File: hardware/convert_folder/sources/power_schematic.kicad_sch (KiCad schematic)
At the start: 33 parts, among them CN1 5-146285-2, CN11 5-146285-2, CN13 4243-0, CN15 JST 2 position header 2.5mm, CN2 4243-0, CN3 4 pin Picoblade, CN7 5-146285-2, CN8 5-146285-2, CN9 5-146285-2, IC1 TPS3780BDBVT, J3 USB-C, J8 87832-1420, J9 87832-1420, SW1 SW-T3-2B-A-A3-S1

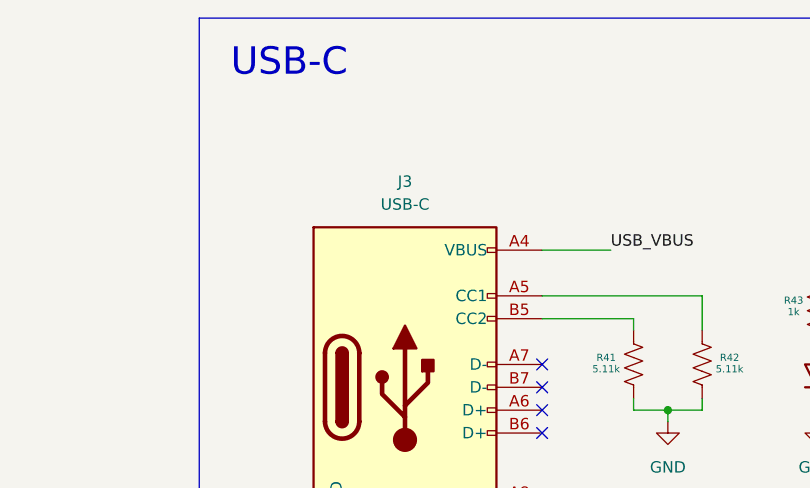
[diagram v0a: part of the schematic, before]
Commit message: fix: fix some footprints and the position of refs. in the layout
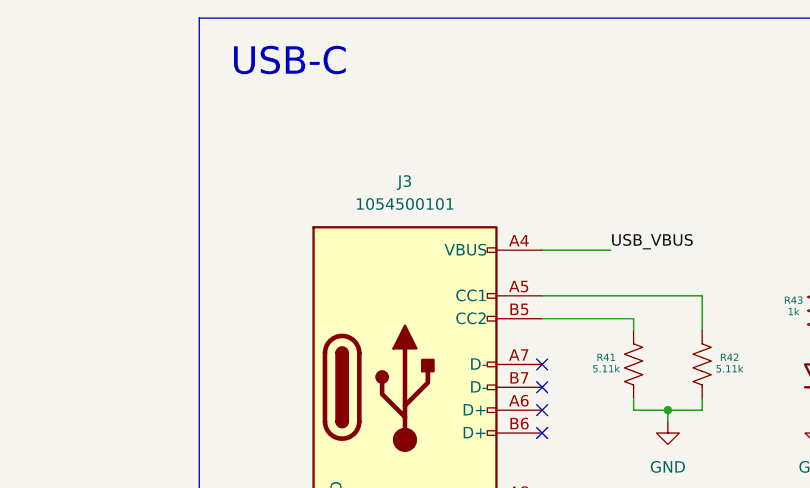
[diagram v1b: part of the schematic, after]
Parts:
- removed J3: USB-C, altium_import:FP-1054500101-MFG, symbol connectors:USB-C
- added J3: 1054500101, altium_import:FP-1054500101-MFG, symbol lib:1054500101
- R41, R42: footprint footprints:RES0402 -> lib:RES0402
- R43: footprint footprints:RES0603 -> lib:RES0603
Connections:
- net GND: now also J3.A1 (GND), J3.A12 (GND), J3.B1 (GND), J3.B12 (GND), J3.S1 (SHIELD)
- net USB_VBUS: now also J3.A4 (VBUS), J3.A9 (VBUS), J3.B4 (VBUS), J3.B9 (VBUS)
- net at R41.2: now also J3.B5 (CC2)
- net at R42.2: now also J3.A5 (CC1)
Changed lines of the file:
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@@
 	(text_box "USB-C"
 		(exclude_from_sim no)
-		(at 242.18 35.941 0)
-		(size -36.44 8.128)
+		(at 205.74 35.941 0)
+		(size 36.44 8.128)
 		(margins 0.9525 0.9525 0.9525 0.9525)
 		(stroke
@@
 			)
 		)
-		(property "Footprint" "footprints:RES0402"
+		(property "Footprint" "lib:RES0402"
 			(at 245.11 50.292 0)
 			(effects
@@
 	)
 	(symbol
-		(lib_id "connectors:USB-C")
-		(at 226.06 74.93 0)
-		(unit 1)
-		(exclude_from_sim no)
-		(in_bom yes)
-		(on_board yes)
-		(dnp no)
-		(fields_autoplaced yes)
-		(property "Reference" "J3"
-			(at 226.06 52.07 0)
-			(effects
-				(font
-					(size 1.27 1.27)
-				)
-			)
-		)
-		(property "Value" "USB-C"
-			(at 226.06 54.61 0)
-			(effects
-				(font
-					(size 1.27 1.27)
-				)
-			)
-		)
-		(property "Footprint" "altium_import:FP-1054500101-MFG"
-			(at 229.87 72.39 0)
-			(effects
-				(font
-					(size 1.27 1.27)
-				)
-				(hide yes)
-			)
-		)
-		(property "Datasheet" "https://www.usb.org/sites/default/files/documents/usb_type-c.zip"
-			(at 273.304 97.028 0)
-			(effects
-				(font
-					(size 1.27 1.27)
-				)
-				(hide yes)
-			)
-		)
-		(property "Description" "USB Power-Only 6P Type-C Receptacle connector"
-			(at 265.684 93.98 0)
-			(effects
-				(font
-					(size 1.27 1.27)
-				)
-				(hide yes)
-			)
-		)
-		(property "Arrow Part Number" ""
-			(at 226.06 74.93 0)
-			(effects
-				(font
-					(size 1.27 1.27)
-				)
-				(hide yes)
-			)
-		)
-		(property "Arrow Price/Stock" ""
-			(at 226.06 74.93 0)
-			(effects
-				(font
-					(size 1.27 1.27)
-				)
-				(hide yes)
-			)
-		)
-		(property "Height" ""
-			(at 226.06 74.93 0)
-			(effects
-				(font
-					(size 1.27 1.27)
-				)
-				(hide yes)
-			)
-		)
-		(property "Manufacturer_Name" ""
-			(at 226.06 74.93 0)
-			(effects
-				(font
-					(size 1.27 1.27)
-				)
-				(hide yes)
-			)
-		)
-		(property "Manufacturer_Part_Number" ""
-			(at 226.06 74.93 0)
-			(effects
-				(font
-					(size 1.27 1.27)
-				)
-				(hide yes)
-			)
-		)
-		(property "Mouser Part Number" ""
-			(at 226.06 74.93 0)
-			(effects
-				(font
-					(size 1.27 1.27)
-				)
-				(hide yes)
-			)
-		)
-		(property "Mouser Price/Stock" ""
-			(at 226.06 74.93 0)
-			(effects
-				(font
-					(size 1.27 1.27)
-				)
-				(hide yes)
-			)
-		)
-		(property "MPN" "UJ20-C-H-G-MSMT-4B-P16-TR"
-			(at 226.06 74.93 0)
-			(effects
-				(font
-					(size 1.27 1.27)
-				)
-				(hide yes)
-			)
-		)
-		(pin "A9"
-		)
-		(pin "S1"
-		)
-		(pin "B12"
-		)
-		(pin "A12"
-		)
-		(pin "B9"
-		)
-		(pin "A5"
-		)
-		(pin "B5"
-		)
-		(pin "B7"
-		)
-		(pin "A6"
-		)
-		(pin "B6"
-		)
-		(pin "A4"
-		)
-		(pin "B4"
-		)
-		(pin "B1"
-		)
-		(pin "A7"
-		)
-		(pin "A1"
-		)
-		(pin "A8"
-		)
-		(pin "B8"
-		)
-		(instances
-			(project "flatsat_platform_2"
-				(path "/8c88a7e1-4137-48d7-b926-b5e762e3852f/8386d232-e6d5-4b15-8289-83f2ee4d46fe"
-					(reference "J3")
-					(unit 1)
-				)
-			)
-		)
-	)
-	(symbol
 		(lib_id "resistors:CRCW06031K00FKEAHP")
 		(at 271.78 66.04 90)
@@
 			)
 		)
-		(property "Footprint" "footprints:RES0603"
+		(property "Footprint" "lib:RES0603"
 			(at 265.43 43.942 0)
 			(effects
@@
 			)
 		)
-		(property "Footprint" "footprints:RES0402"
+		(property "Footprint" "lib:RES0402"
 			(at 252.73 50.292 0)
 			(effects
@@
 					(unit 1)
 				)
+			)
+		)
+	)
+	(symbol
+		(lib_id "lib:1054500101")
+		(at 226.06 74.93 0)
+		(unit 1)
+		(exclude_from_sim no)
+		(in_bom yes)
+		(on_board yes)
+		(dnp no)
+		(fields_autoplaced yes)
+		(property "Reference" "J3"
+			(at 226.06 52.07 0)
+			(effects
+				(font
+					(size 1.27 1.27)
+				)
+			)
+		)
+		(property "Value" "1054500101"
+			(at 226.06 54.61 0)
+			(effects
+				(font
+					(size 1.27 1.27)
+				)
+			)
+		)
+		(property "Footprint" "altium_import:FP-1054500101-MFG"
+			(at 229.87 72.39 0)
+			(effects
+				(font
+					(size 1.27 1.27)
+				)
+				(hide yes)
+			)
+		)
+		(property "Datasheet" "https://www.usb.org/sites/default/files/documents/usb_type-c.zip"
+			(at 273.304 97.028 0)
+			(effects
+				(font
+					(size 1.27 1.27)
+				)
+				(hide yes)
+			)
+		)
+		(property "Description" "USB Power-Only 6P Type-C Receptacle connector"
+			(at 265.684 93.98 0)
+			(effects
+				(font
+					(size 1.27 1.27)
+				)
+				(hide yes)
+			)
+		)
+		(property "Arrow Part Number" ""
+			(at 226.06 74.93 0)
+			(effects
+				(font
+					(size 1.27 1.27)
+				)
+				(hide yes)
+			)
+		)
+		(property "Arrow Price/Stock" ""
+			(at 226.06 74.93 0)
+			(effects
+				(font
+					(size 1.27 1.27)
+				)
+				(hide yes)
+			)
+		)
+		(property "Height" ""
+			(at 226.06 74.93 0)
+			(effects
+				(font
+					(size 1.27 1.27)
+				)
+				(hide yes)
+			)
+		)
+		(property "Manufacturer_Name" ""
+			(at 226.06 74.93 0)
+			(effects
+				(font
+					(size 1.27 1.27)
+				)
+				(hide yes)
+			)
+		)
+		(property "Manufacturer_Part_Number" ""
+			(at 226.06 74.93 0)
+			(effects
+				(font
+					(size 1.27 1.27)
+				)
+				(hide yes)
+			)
+		)
+		(property "Mouser Part Number" ""
+			(at 226.06 74.93 0)
+			(effects
+				(font
+					(size 1.27 1.27)
+				)
+				(hide yes)
+			)
+		)
+		(property "Mouser Price/Stock" ""
+			(at 226.06 74.93 0)
+			(effects
+				(font
+					(size 1.27 1.27)
+				)
+				(hide yes)
+			)
+		)
+		(property "MPN" "UJ20-C-H-G-MSMT-4B-P16-TR"
+			(at 226.06 74.93 0)
+			(effects
+				(font
+					(size 1.27 1.27)
+				)
+				(hide yes)
+			)
+		)
+		(pin "B7"
+		)
+		(pin "A8"
+		)
+		(pin "A1"
+		)
+		(pin "S1"
+		)
+		(pin "A4"
+		)
+		(pin "B12"
+		)
+		(pin "B6"
+		)
+		(pin "B8"
+		)
+		(pin "A6"
+		)
+		(pin "B4"
+		)
+		(pin "B5"
+		)
+		(pin "A7"
+		)
+		(pin "B9"
+		)
+		(pin "B1"
+		)
+		(pin "A9"
+		)
+		(pin "A12"
+		)
+		(pin "A5"
+		)
+		(instances
+			(project "flatsat_platform_2"
+				(path "/8c88a7e1-4137-48d7-b926-b5e762e3852f/8386d232-e6d5-4b15-8289-83f2ee4d46fe"
+					(reference "J3")
+					(unit 1)
+				)

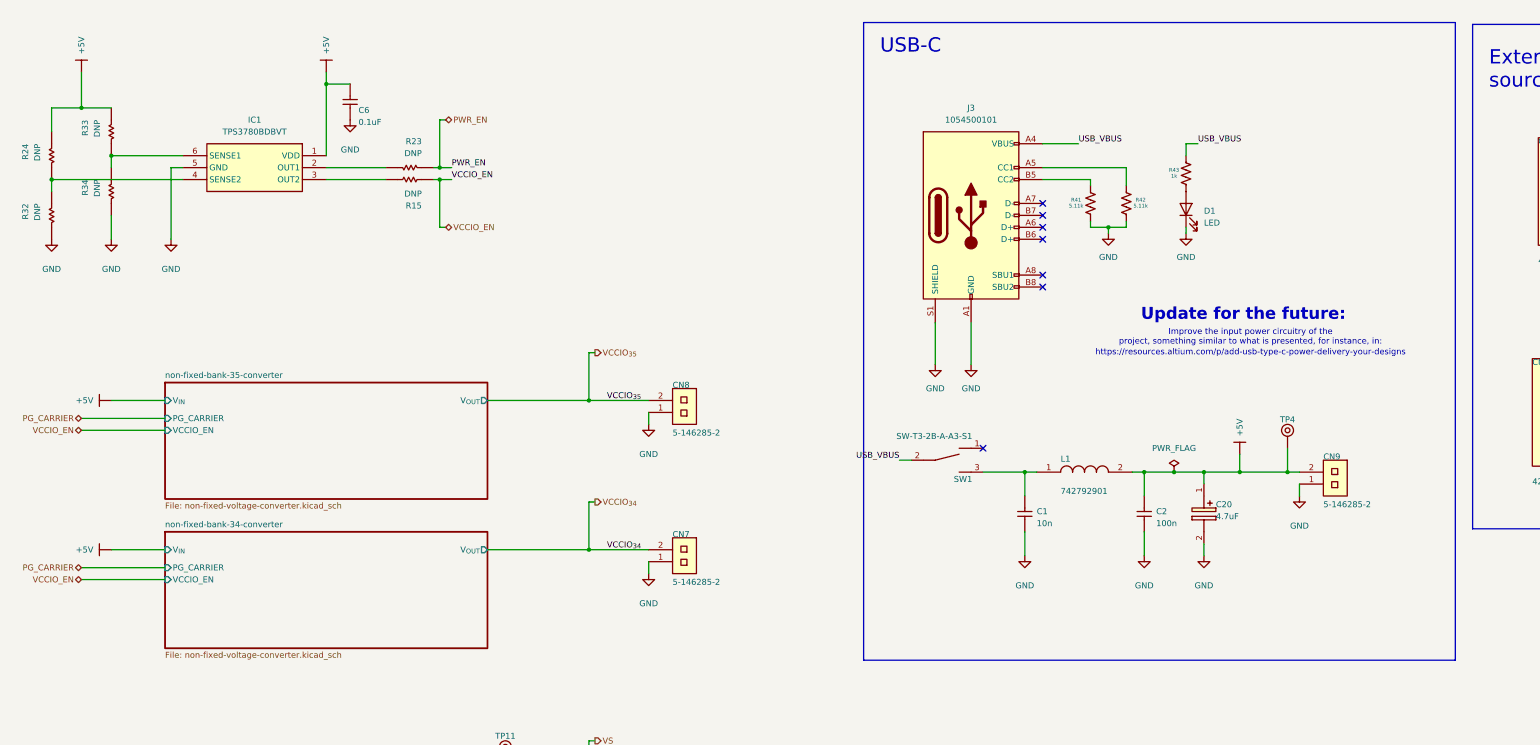
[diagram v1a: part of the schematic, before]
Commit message: fix: minor corrections at the TPS3780 circuit
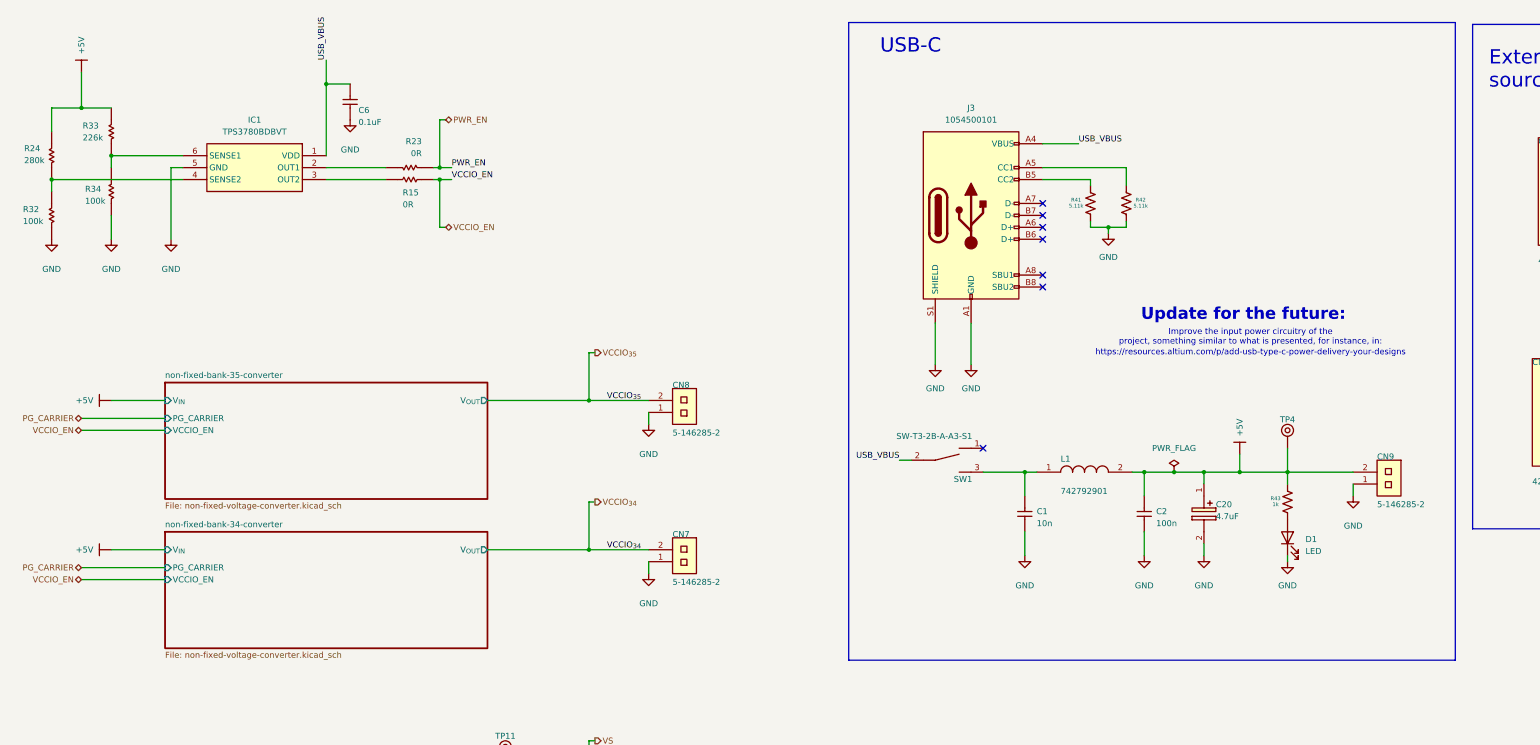
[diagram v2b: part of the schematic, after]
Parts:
- R15, R23: value DNP -> 0R
- R24: value DNP -> 280k
- R32, R34: value DNP -> 100k
- R33: value DNP -> 226k
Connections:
- net +5V: now also R43.2; no longer C6.1, IC1.1 (VDD)
- net USB_VBUS: now also C6.1, IC1.1 (VDD); no longer R43.2
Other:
- moved on the sheet: CN9, D1, R43

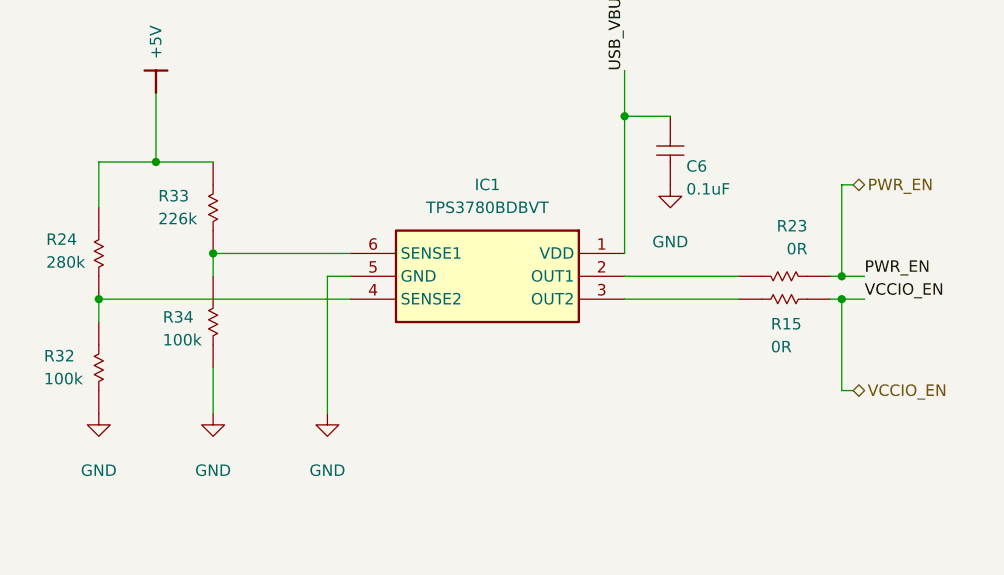
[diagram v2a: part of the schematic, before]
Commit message: fix: fix caps. values, add decoupling capacitors for INAs and other ICs, and add general improvements
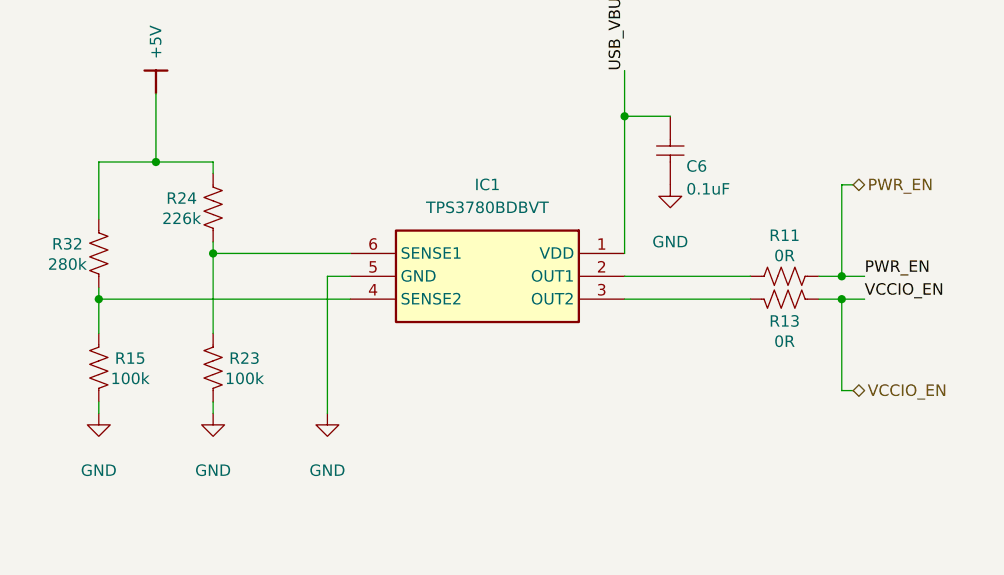
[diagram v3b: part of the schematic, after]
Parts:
- removed R15, R23: 0R, altium_import:0805, symbol altium_import:RDNP_0805
- removed R24: 280k, altium_import:0805, symbol altium_import:RDNP_0805
- removed R32, R34: 100k, altium_import:0805, symbol altium_import:RDNP_0805
- removed R33: 226k, altium_import:0805, symbol altium_import:RDNP_0805
- added R11, R13: 0R, lib:RES0805, symbol resistors:CRCW08050000Z0EAHP
- added R15, R23: 100k, lib:RES0805, symbol resistors:CRCW0805100KFKEAHP
- added R24: 226k, lib:RES0805, symbol resistors:CRCW0805226KFKEAHP
- added R32: 280k, lib:RES0805, symbol resistors:CRCW0805280KFKEAHP
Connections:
- net +5V: now also R24.2, R32.2
- net GND: now also R15.1, R23.1
- net PWR_EN: now also R11.2
- net VCCIO_EN: now also R13.2
- net at IC1.2 (OUT1): now also R11.1
- net at IC1.6 (SENSE1): now also R23.2, R24.1
- net at IC1.4 (SENSE2): now also R15.2, R32.1
- net at IC1.3 (OUT2): now also R13.1
